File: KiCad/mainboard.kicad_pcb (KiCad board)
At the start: 2 copper layers, 139.7 x 83.8 mm, 60 parts, among them J1 Arduino_Nano_Header, P1 CONN_02X13, P2 CONN_02X13, P3 USB_B, P4 CONN_01X04, P5 CONN_01X02, P6 CONN_01X02, P7 CONN_01X02, U1 74LS165, U2 74LS165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

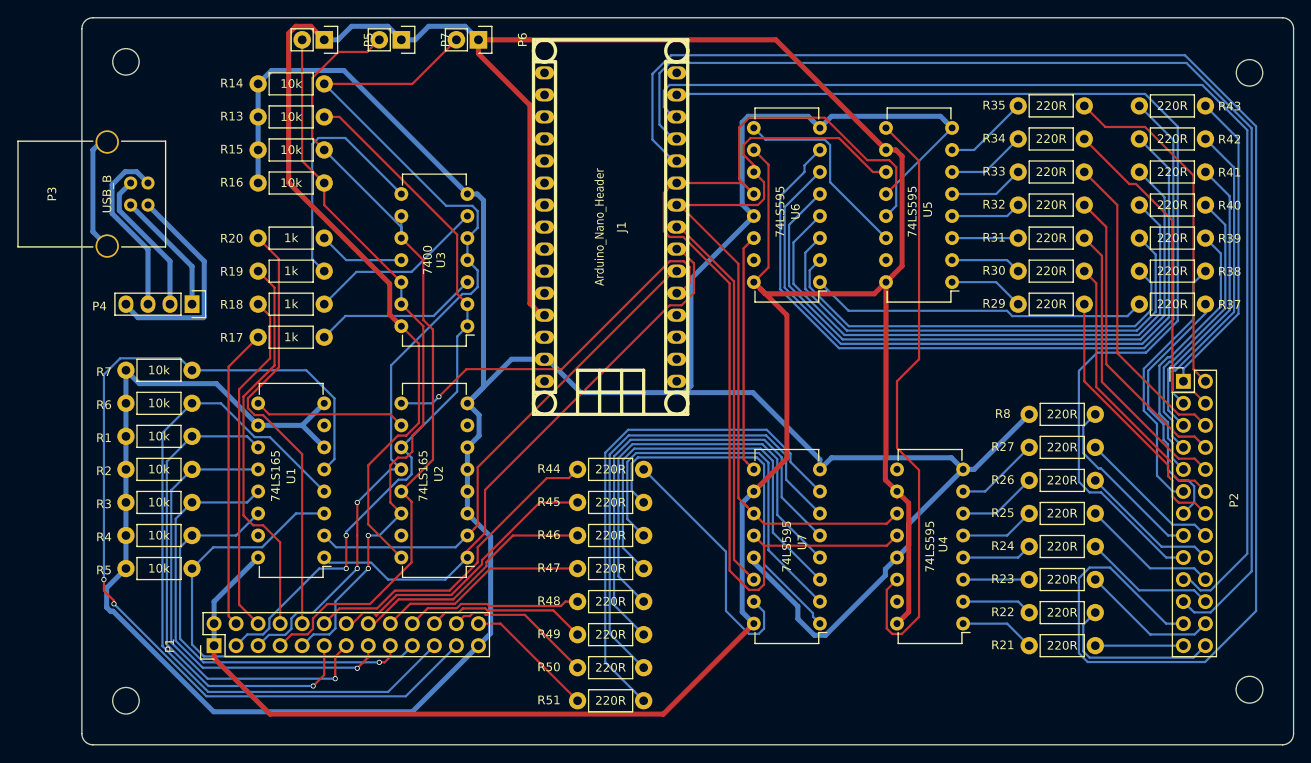
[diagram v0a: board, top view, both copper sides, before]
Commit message: Added four missing LED-resistors and ...
... turned Arduino again. That was necessary because the connector must not be
at the edge of the PCB.
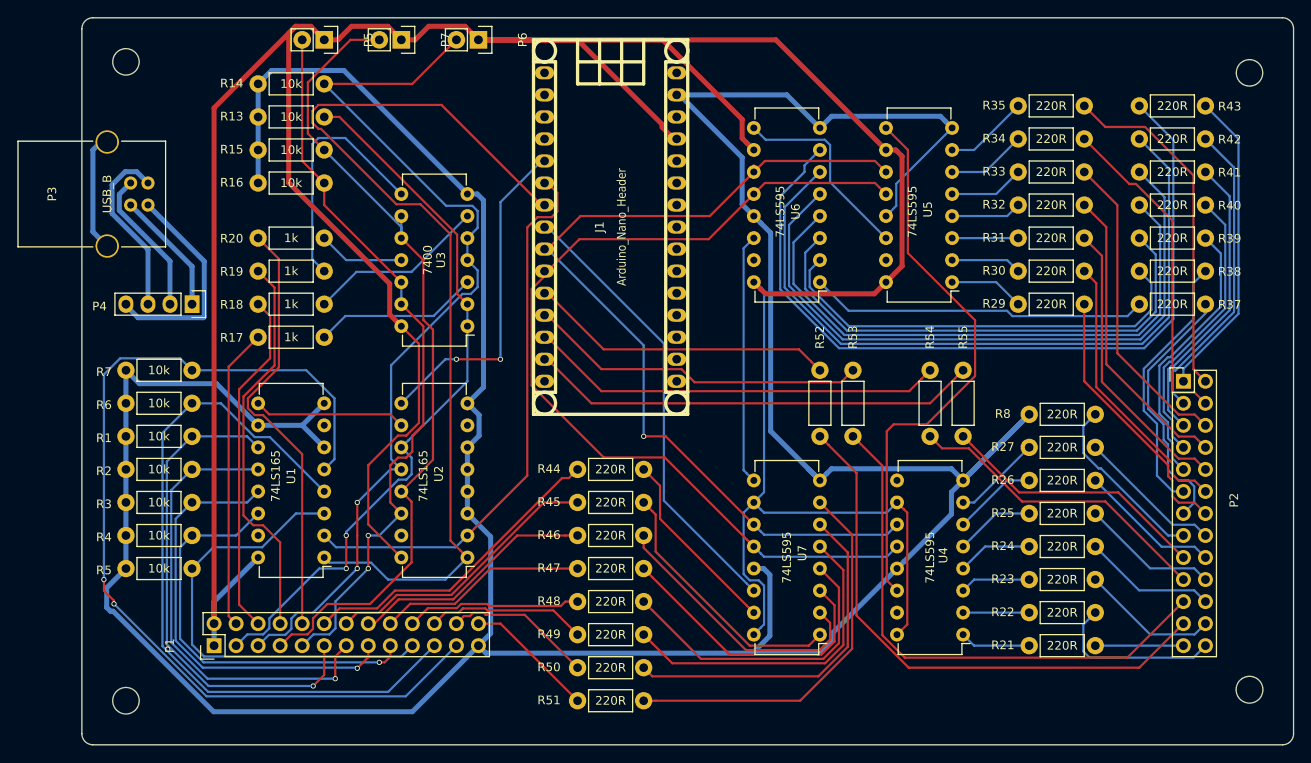
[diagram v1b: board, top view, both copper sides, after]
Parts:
- added R52: 1k, Resistors_ThroughHole:Resistor_Horizontal_RM7mm, F.Cu at (174.0, 78.7)
- added R53: 1k, Resistors_ThroughHole:Resistor_Horizontal_RM7mm, F.Cu at (177.8, 78.7)
- added R54: 1k, Resistors_ThroughHole:Resistor_Horizontal_RM7mm, F.Cu at (186.7, 78.7)
- added R55: 1k, Resistors_ThroughHole:Resistor_Horizontal_RM7mm, F.Cu at (190.5, 78.7)
- moved U4 1.27 mm to (190.5, 109.2)
- moved U7 1.27 mm to (174.0, 109.2)
- turned J1 to 270 degrees
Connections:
- P2 pad 17: Net-(J1-Pad14) -> Net-(P2-Pad17)
- P2 pad 19: Net-(J1-Pad13) -> Net-(P2-Pad19)
- P2 pad 21: Net-(J1-Pad12) -> Net-(P2-Pad21)
- P2 pad 23: Net-(J1-Pad11) -> Net-(P2-Pad23)
- P3 pad 5: Net-(P3-Pad5) -> GND
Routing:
- net Net-(J1-Pad11): track 188.3 -> 35.4 mm
- net Net-(J1-Pad12): track 142.6 -> 39.7 mm
- net Net-(J1-Pad13): track 132.0 -> 48.0 mm
- net Net-(J1-Pad14): track 125.4 -> 52.6 mm
- net Net-(P2-Pad23): track 0.00 -> 64.7 mm
- net Net-(P2-Pad21): track 0.00 -> 62.8 mm
- net Net-(J1-Pad7): track 66.1 -> 111.1 mm
- net GND: track 400.7 -> 442.1 mm, vias 0 -> 1
- net Net-(P2-Pad19): track 0.00 -> 36.8 mm
- net Net-(P2-Pad17): track 0.00 -> 31.9 mm
- net Net-(R49-Pad1): track 53.8 -> 37.7 mm
- net Net-(R50-Pad1): track 56.7 -> 40.8 mm
- net Net-(R48-Pad1): track 50.8 -> 35.5 mm
- net Net-(R51-Pad1): track 59.8 -> 44.9 mm
- net Net-(R47-Pad1): track 47.9 -> 33.3 mm
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
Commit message: Made CLK INH (Pin 15) of the 74HC165s LO
The input shift registers turned out to have a strong tendency to disturbance
and their signals were very unstable. The manual of 74HC165 says, that all
the unused input pins should be either at GND or VCC. For the CLK INH
(clock inhibit) VCC is not an option, as this would inhibit the clock.
Therefore we put them to GND.

It turns out to be far more stable.
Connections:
- U1 pad 15: Net-(U1-Pad15) -> GND
- U2 pad 15: Net-(U2-Pad15) -> GND
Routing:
- net GND: track 442.1 -> 466.7 mm, vias 1 -> 2
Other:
- net class small gnd vcc added: clearance 0.254, trace_width 0.254, via_dia 0.6, via_drill 0.4

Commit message: Added capacitors to ICs
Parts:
- added C1: 100nF, Capacitors_ThroughHole:C_Disc_D3_P2.5, F.Cu at (120.7, 88.9)
- added C2: 100nF, Capacitors_ThroughHole:C_Disc_D3_P2.5, F.Cu at (137.2, 88.9)
- added C4: 100nF, Capacitors_ThroughHole:C_Disc_D3_P2.5, F.Cu at (185.4, 115.6)
- added C5: 100nF, Capacitors_ThroughHole:C_Disc_D3_P2.5, F.Cu at (177.8, 63.5)
- added C6: 100nF, Capacitors_ThroughHole:C_Disc_D3_P2.5, F.Cu at (162.6, 67.3)
- added C7: 100nF, Capacitors_ThroughHole:C_Disc_D3_P2.5, F.Cu at (162.6, 109.3)
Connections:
- P3 pad 4: Net-(P3-Pad4) -> GND
- P4 pad 1: Net-(P3-Pad4) -> GND
- R8 pad 1: Net-(P2-Pad15) -> GND
- R8 pad 2: GND -> Net-(P2-Pad15)
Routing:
- net GND: track 466.7 -> 524.3 mm
- net VCC: track 416.3 -> 437.4 mm
- net Net-(P3-Pad4): track 14.4 -> 0.00 mm
- net Net-(R46-Pad1): track 31.9 -> 36.6 mm
- net Net-(R49-Pad1): track 37.7 -> 41.9 mm
- net Net-(R47-Pad1): track 33.3 -> 37.1 mm
- net Net-(P2-Pad15): track 20.5 -> 17.0 mm
- net Net-(R50-Pad1): track 40.8 -> 44.1 mm
- net Net-(R48-Pad1): track 35.5 -> 38.2 mm
- net Net-(R45-Pad1): track 30.2 -> 27.7 mm
- net Net-(R51-Pad1): track 44.9 -> 46.5 mm

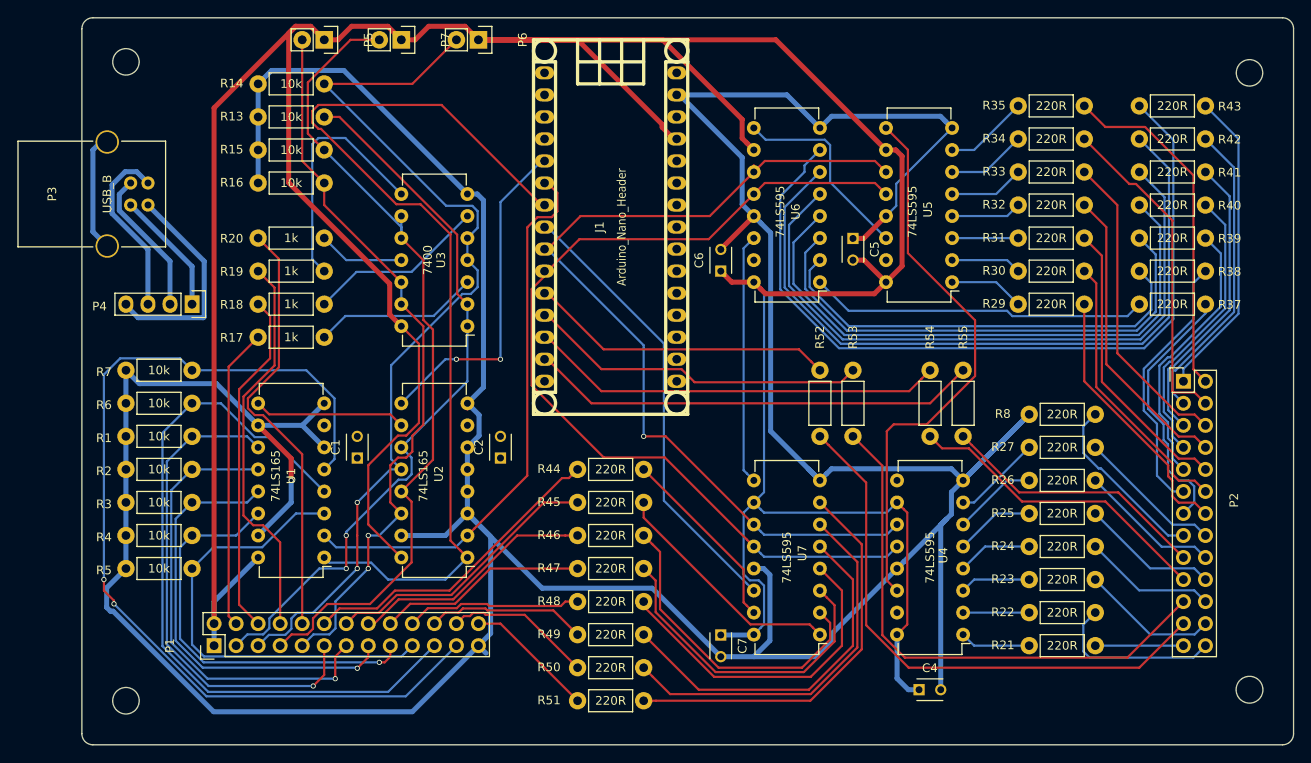
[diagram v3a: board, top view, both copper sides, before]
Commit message: KiCad update; wiring of denoising capacitors
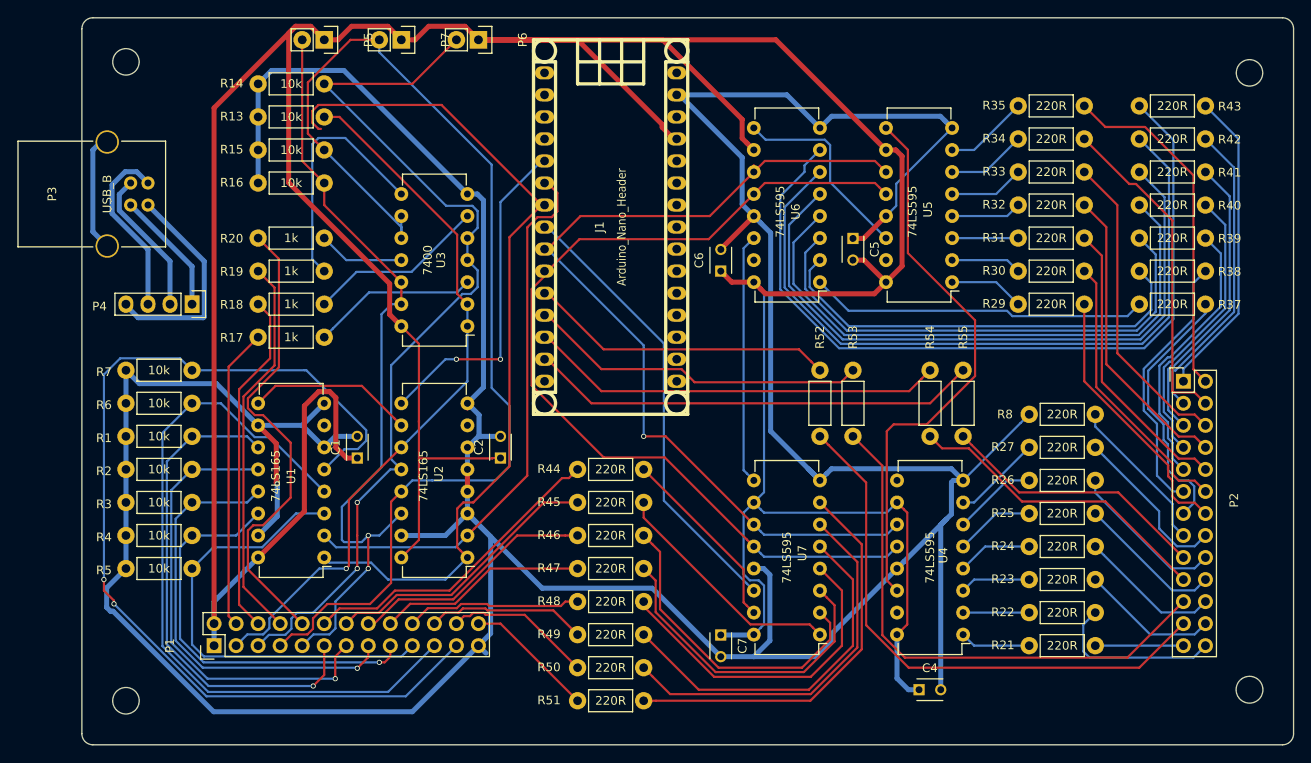
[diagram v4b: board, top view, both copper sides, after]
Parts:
- moved R8 7.62 mm to (198.1, 83.8), turned to 0 degrees
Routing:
- net VCC: track 437.4 -> 476.3 mm
- net Net-(P1-Pad7): track 96.0 -> 131.8 mm
- net Net-(J1-Pad7): track 111.1 -> 98.9 mm
- net GND: track 524.3 -> 516.1 mm
- net Net-(P1-Pad9): track 84.9 -> 91.2 mm
- net Net-(P1-Pad10): track 50.1 -> 54.8 mm
- net Net-(P1-Pad23): track 111.2 -> 115.1 mm
- net Net-(P2-Pad16): track 17.6 -> 19.8 mm
- net Net-(P2-Pad18): track 17.1 -> 18.9 mm
- net Net-(U1-Pad9): track 17.6 -> 19.2 mm
- net Net-(P1-Pad3): track 84.3 -> 82.8 mm, vias 2 -> 1
- net Net-(P2-Pad15): track 17.0 -> 18.2 mm
- net Net-(P2-Pad22): track 15.3 -> 16.4 mm
- net Net-(P2-Pad20): track 15.9 -> 16.9 mm
- net Net-(P1-Pad8): track 45.3 -> 44.7 mm
